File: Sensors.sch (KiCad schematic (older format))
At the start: 40 parts, among them CON1 CONSOLE, P1 CONN_02X20, P10 CBUS, P11 I2C0, P12 I2C0, P13 I2C1, P14 I2C1, P7 96B_SPI, U1 CJT1117-3.3, U2 XC6206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

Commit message: Add MOSFETs to switch power supply between 3.3V and 5V
The original design just routed the power rails directly through solder
jumper pads, but feedback from review suggested that a switch would be
more friendly to end users. The power rails could have been routed
directly through a physical switch, but I was concerned about noise on
the power rails. Instead, add power supply switching by routing the 5V
and 3.3V rails through a pair of MOSFETs to isolate them from a switch
or jumper pads.

Signed-off-by: Grant Likely <grant.likely@linaro.org>
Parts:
- removed GS1: GS3, Connect:GS3, symbol GS3
- added C17, C18: 100n, Capacitors_SMD:C_0603, symbol C_Small
- added Q2, Q3: CJ2305, Housings_SOT-23_SOT-143_TSOT-6:SOT-23, symbol CJ2305
- added R19, R20: 100k, Sensors:R_0603_Seeed, symbol R
- added SW1: VIO, Sensors:DIP_Toggle_Switch, symbol Switch_SPDT_x2
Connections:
- wire segments 154 -> 173
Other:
- moved on the sheet: C1, C2, U1

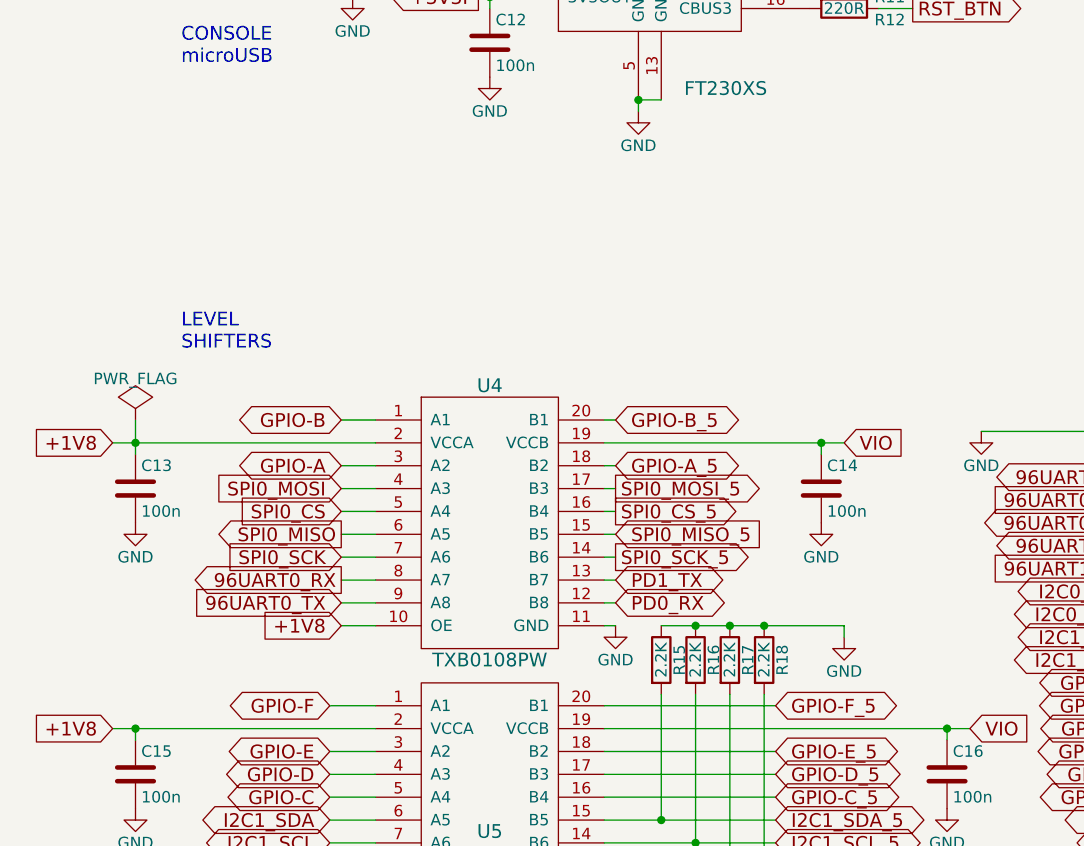
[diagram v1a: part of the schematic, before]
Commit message: Pull i2c lines UP, not down
The schematic was wrong. It was pulling the i2c lines down instead of
up. Fix both the schematic and the layout.

Signed-off-by: Grant Likely <grant.likely@linaro.org>
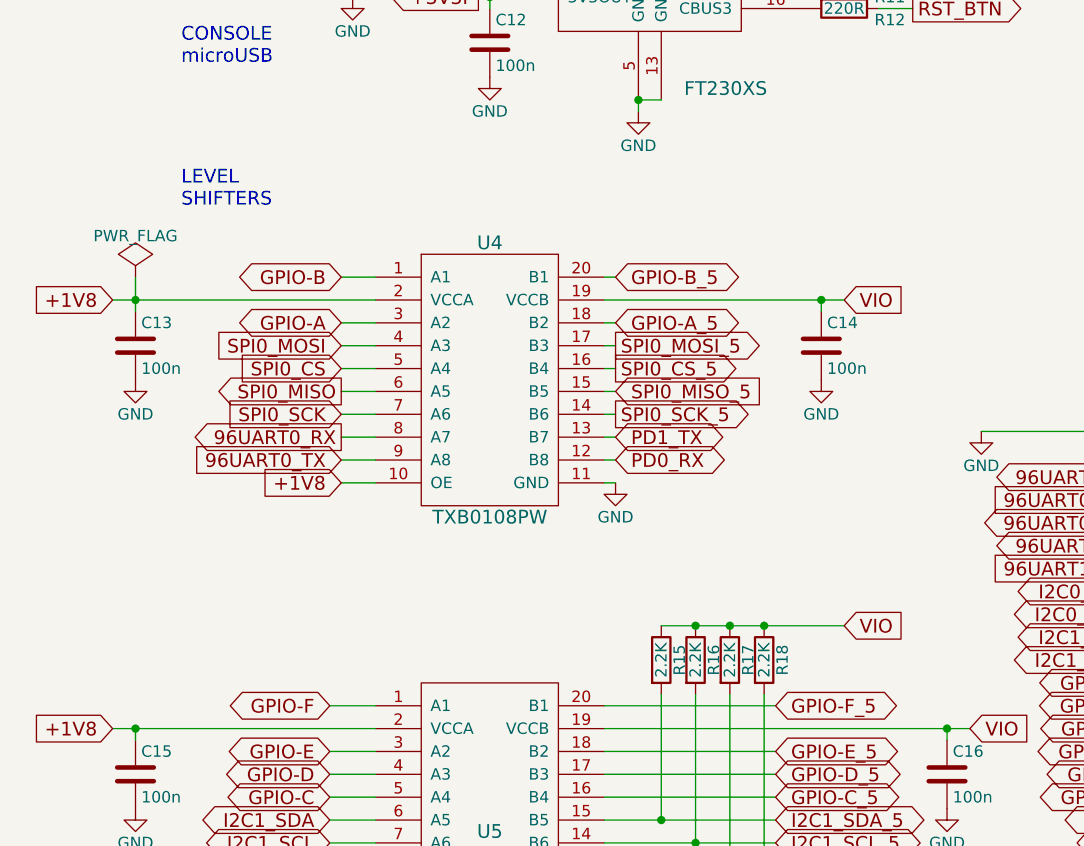
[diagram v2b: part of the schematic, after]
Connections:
- net GND: no longer R15.1, R16.1, R17.1, R18.1
- net VIO: now also R15.1, R16.1, R17.1, R18.1
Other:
- moved on the sheet: C13, C14, U4

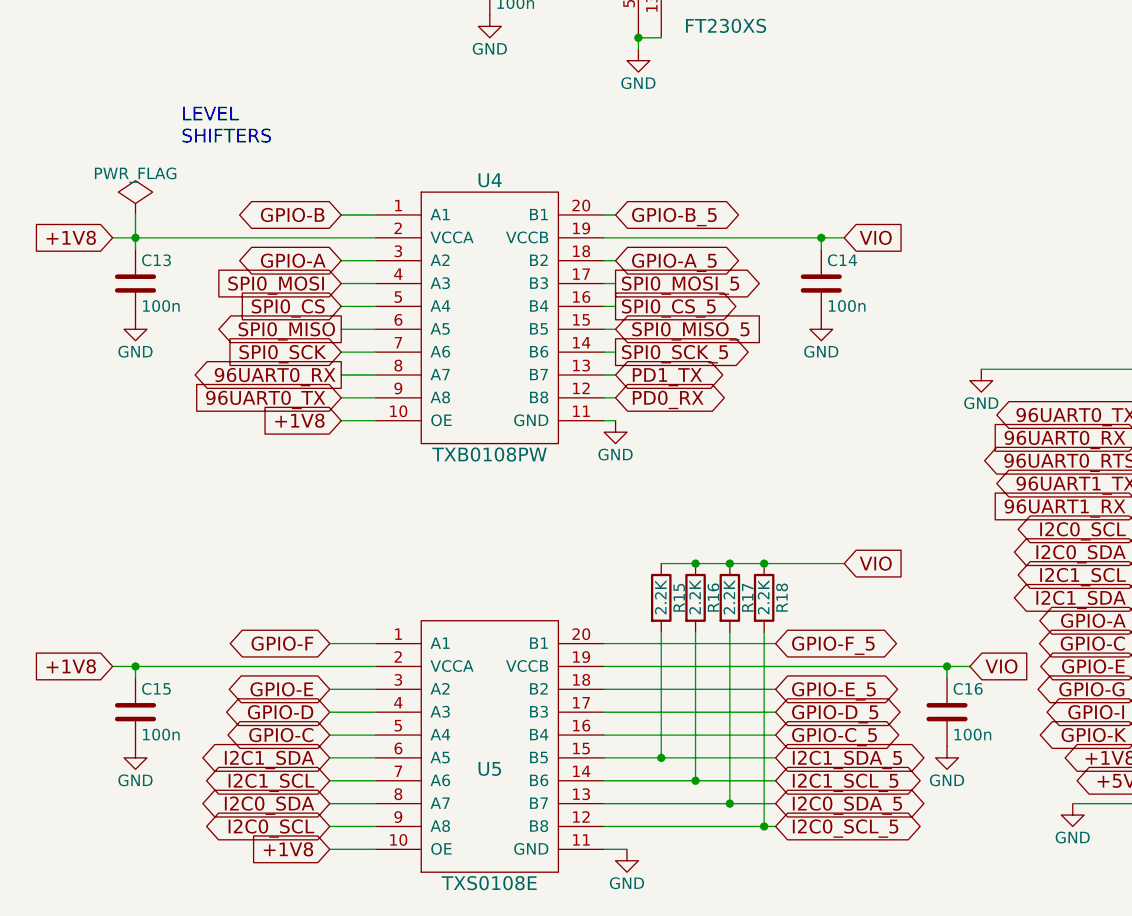
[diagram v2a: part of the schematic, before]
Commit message: Add pads for i2c pull ups on the 1.8V side
It isn't yet known if we'll need them, but add pads for pullup resistors
on the i2c 1.8V lines. Doing so ensures that we won't need to respin the
board if the pullups turn out to be required.

Signed-off-by: Grant Likely <grant.likely@linaro.org>
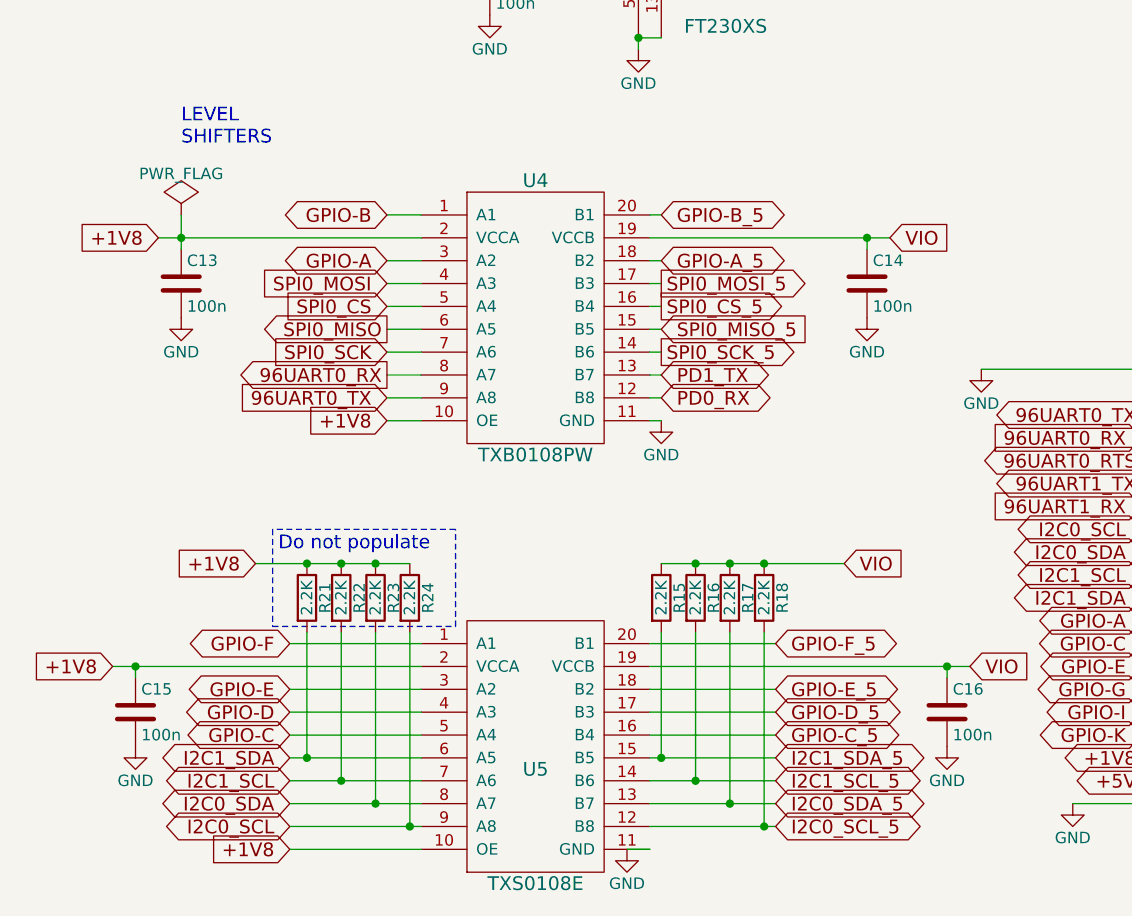
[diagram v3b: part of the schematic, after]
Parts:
- added R21, R22, R23, R24: 2.2K, Sensors:R_0603_Seeed, symbol R
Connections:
- net +1V8: now also R21.1, R22.1, R23.1, R24.1
- net I2C0_SCL: now also R24.2
- net I2C0_SDA: now also R23.2
- net I2C1_SCL: now also R22.2
- net I2C1_SDA: now also R21.2
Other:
- note added: "Do not populate"
- moved on the sheet: C13, C14, U4, U5

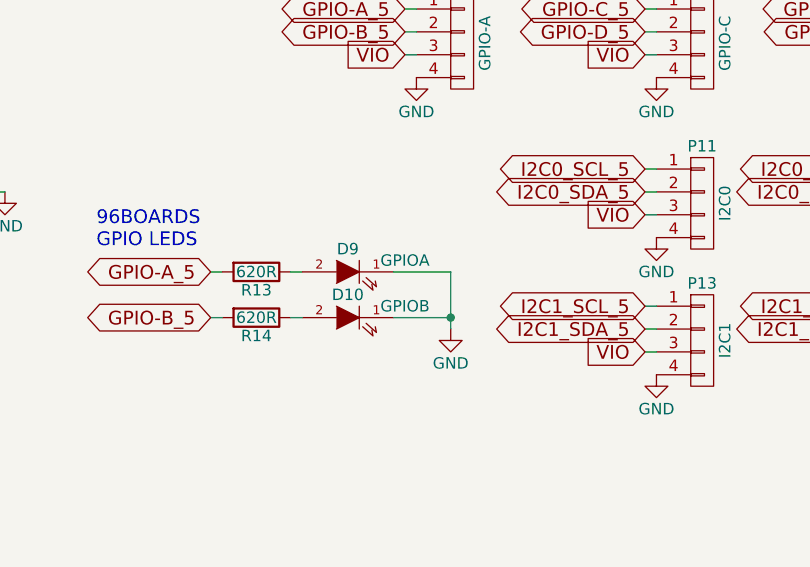
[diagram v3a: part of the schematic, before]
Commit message: Fix up silkscreen by making labels smaller
Change all the R and C labels, plus a few more, to 0.7 point instead of
1 to make everything less cramped.

Signed-off-by: Grant Likely <grant.likely@linaro.org>
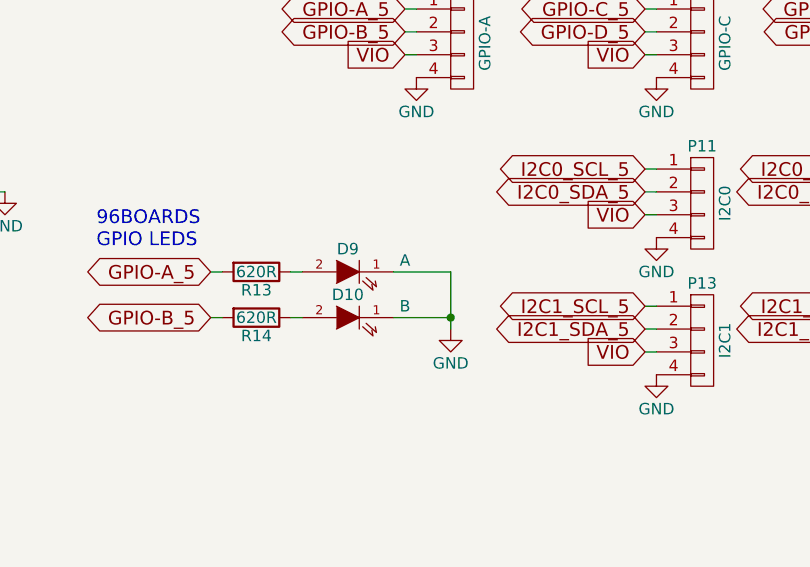
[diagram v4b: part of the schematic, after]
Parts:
- D10: value GPIOB -> B
- D9: value GPIOA -> A
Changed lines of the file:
@@
 P 8300 5850
 F 0 "D9" H 8300 5950 50  0000 C CNN
-F 1 "GPIOA" H 8050 5900 50  0000 C CNN
+F 1 "A" H 8050 5900 50  0000 C CNN
 F 2 "LEDs:LED-0603" H 8300 5850 60  0001 C CNN
 F 3 "" H 8300 5850 60  0000 C CNN
@@
 P 8300 6050
 F 0 "D10" H 8300 6150 50  0000 C CNN
-F 1 "GPIOB" H 8050 6100 50  0000 C CNN
+F 1 "B" H 8050 6100 50  0000 C CNN
 F 2 "LEDs:LED-0603" H 8300 6050 60  0001 C CNN
 F 3 "" H 8300 6050 60  0000 C CNN
